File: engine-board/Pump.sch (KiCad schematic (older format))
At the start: 12 parts, among them J301 Steering Turbines, J302 MAXON Pump Controller, J303 Pump Current Sensor, J304 VL6180 Range Sensor, J305 Turbine 1 ESC, J306 Turbine 2 ESC, J307 Turbine Current Sensor, J308 Solenoid Current Sensor, J309 Solenoid, Q301 IRLB8721PBF

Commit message: pcb parts done, footprints updated, ready for routing
pre-routing step..
- finalized footprints
- verified layout, size, mounting holes (1.75" apart)
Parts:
- removed J303: Pump Current Sensor, Connector_PinSocket_2.54mm:PinSocket_1x06_P2.54mm_Vertical, symbol Connector:Conn_01x06_Female
- removed J307: Turbine Current Sensor, Connector_PinSocket_2.54mm:PinSocket_1x06_P2.54mm_Vertical, symbol Connector:Conn_01x06_Female
- removed J308: Solenoid Current Sensor, Connector_PinSocket_2.54mm:PinSocket_1x06_P2.54mm_Vertical, symbol Connector:Conn_01x06_Female
- added J303: Pump Current Sensor, Connector_PinSocket_2.54mm:PinSocket_1x08_P2.54mm_Vertical, symbol Connector:Conn_01x08_Female
- added J307: Turbine Current Sensor, Connector_PinSocket_2.54mm:PinSocket_1x08_P2.54mm_Vertical, symbol Connector:Conn_01x08_Female
- added J308: Solenoid Current Sensor, Connector_PinSocket_2.54mm:PinSocket_1x08_P2.54mm_Vertical, symbol Connector:Conn_01x08_Female
- added TP301: TP_SolGate, TestPoint:TestPoint_Loop_D2.60mm_Drill1.6mm_Beaded, symbol engine-board-eagle-import:TEST-POINTTP_15TH_THRU
- added TP302: TP_SolVolt, TestPoint:TestPoint_Loop_D2.60mm_Drill1.6mm_Beaded, symbol engine-board-eagle-import:TEST-POINTTP_15TH_THRU
- added TP304: TP_SolBat+, TestPoint:TestPoint_Loop_D2.60mm_Drill1.6mm_Beaded, symbol engine-board-eagle-import:TEST-POINTTP_15TH_THRU
- renumbered J302 to J1
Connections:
- wire segments 90 -> 96

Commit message: shortend pcb, ready to route
ready to route, shortend pcb, layout complete
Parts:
- removed TP301: TP_SolGate, TestPoint:TestPoint_Loop_D2.60mm_Drill1.6mm_Beaded, symbol engine-board-eagle-import:TEST-POINTTP_15TH_THRU
- removed TP302: TP_SolVolt, TestPoint:TestPoint_Loop_D2.60mm_Drill1.6mm_Beaded, symbol engine-board-eagle-import:TEST-POINTTP_15TH_THRU
- removed TP304: TP_SolBat+, TestPoint:TestPoint_Loop_D2.60mm_Drill1.6mm_Beaded, symbol engine-board-eagle-import:TEST-POINTTP_15TH_THRU
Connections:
- wire segments 96 -> 93
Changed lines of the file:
@@
 Text HLabel 900  3200 2    50   Input ~ 0
 pump_motor_analog_gnd
-Text HLabel 7950 1000 0    50   Input ~ 0
+Text HLabel 7950 950  0    50   Input ~ 0
 solenoid_mosfet_gate
 $Comp
@@
 	1950 2700 1950 2250
 Connection ~ 2650 2700
-$Comp
-L engine-board-eagle-import:TEST-POINTTP_15TH_THRU TP?
-U 1 1 61D301E8
-P 9600 2000
-AR Path="/61D301E8" Ref="TP?"  Part="1"
-AR Path="/618F9F5D/61D301E8" Ref="TP?"  Part="1"
-AR Path="/619906DF/61D301E8" Ref="TP304"  Part="1"
-F 0 "TP304" H 9644 2240 70  0000 C CNN
-F 1 "TP_SolBat+" H 9644 2119 70  0000 C CNN
-F 2 "TestPoint:TestPoint_Loop_D2.60mm_Drill1.6mm_Beaded" H 9600 2000 50  0001 C CNN
-F 3 "https://www.keyelco.com/userAssets/file/M65p64.pdf" H 9600 2000 50  0001 C CNN
-F 4 "0.23" H 9600 2000 50  0001 C CNN "Price"
-F 5 "680" H 9600 2000 50  0001 C CNN "MFN"
-F 6 "https://www.digikey.com/en/products/detail/keystone-electronics/680/316581" H 9600 2000 50  0001 C CNN "Link"
-	1    9600 2000
-	1    0    0    -1
-$EndComp
-Wire Wire Line
-	9100 1700 9100 2000
-Wire Wire Line
-	9100 2000 9600 2000
-Connection ~ 9100 1700
-$Comp
-L engine-board-eagle-import:TEST-POINTTP_15TH_THRU TP?
-U 1 1 61D3D5E1
-P 9300 1200
-AR Path="/61D3D5E1" Ref="TP?"  Part="1"
-AR Path="/618F9F5D/61D3D5E1" Ref="TP?"  Part="1"
-AR Path="/619906DF/61D3D5E1" Ref="TP302"  Part="1"
-F 0 "TP302" H 9350 1450 70  0000 C CNN
-F 1 "TP_SolVolt" H 9344 1319 70  0000 C CNN
-F 2 "TestPoint:TestPoint_Loop_D2.60mm_Drill1.6mm_Beaded" H 9300 1200 50  0001 C CNN
-F 3 "https://www.keyelco.com/userAssets/file/M65p64.pdf" H 9300 1200 50  0001 C CNN
-F 4 "0.23" H 9300 1200 50  0001 C CNN "Price"
-F 5 "680" H 9300 1200 50  0001 C CNN "MFN"
-F 6 "https://www.digikey.com/en/products/detail/keystone-electronics/680/316581" H 9300 1200 50  0001 C CNN "Link"
-	1    9300 1200
-	1    0    0    -1
-$EndComp
 Connection ~ 9200 1200
-$Comp
-L engine-board-eagle-import:TEST-POINTTP_15TH_THRU TP?
-U 1 1 61D4B1C3
-P 8100 950
-AR Path="/61D4B1C3" Ref="TP?"  Part="1"
-AR Path="/618F9F5D/61D4B1C3" Ref="TP?"  Part="1"
-AR Path="/619906DF/61D4B1C3" Ref="TP301"  Part="1"
-F 0 "TP301" H 8144 1190 70  0000 C CNN
-F 1 "TP_SolGate" H 8144 1069 70  0000 C CNN
-F 2 "TestPoint:TestPoint_Loop_D2.60mm_Drill1.6mm_Beaded" H 8100 950 50  0001 C CNN
-F 3 "https://www.keyelco.com/userAssets/file/M65p64.pdf" H 8100 950 50  0001 C CNN
-F 4 "0.23" H 8100 950 50  0001 C CNN "Price"
-F 5 "680" H 8100 950 50  0001 C CNN "MFN"
-F 6 "https://www.digikey.com/en/products/detail/keystone-electronics/680/316581" H 8100 950 50  0001 C CNN "Link"
-	1    8100 950
-	1    0    0    -1
-$EndComp
 Wire Wire Line
 	9300 1200 9200 1200
 Wire Wire Line
-	7950 950  8100 950
-Wire Wire Line
 	7950 950  7950 1300

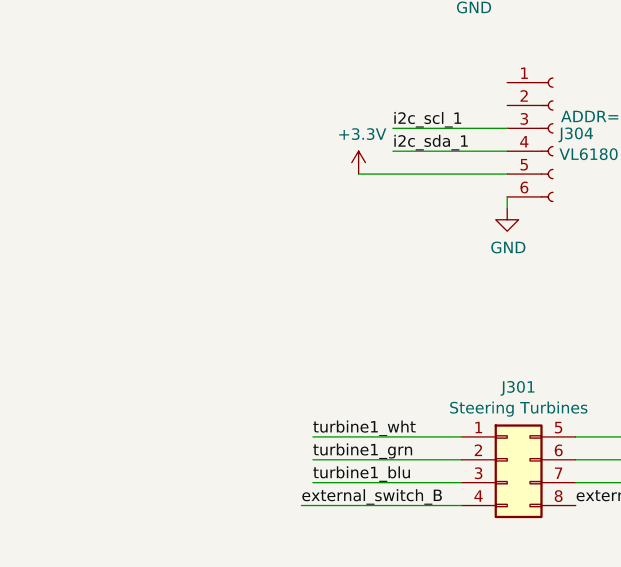
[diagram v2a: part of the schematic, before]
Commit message: ready for layout
- added batt solder tabs
- swapped some terminal blocks with microfit connectors
- shortened board, tightened layout
- tried to space everything out properly
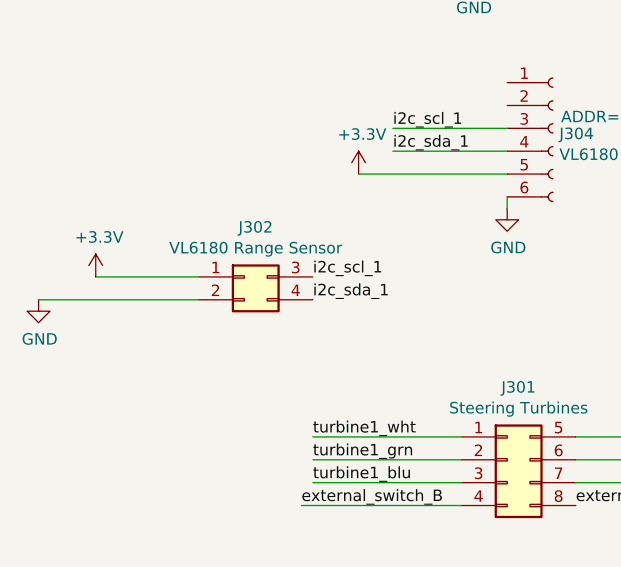
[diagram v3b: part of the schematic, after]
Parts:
- added J302: VL6180 Range Sensor, Connector_Molex:Molex_Micro-Fit_3.0_43045-0421_2x02-1MP_P3.00mm_Horizontal, symbol Connector_Generic:Conn_02x02_Top_Bottom
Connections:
- wire segments 93 -> 95
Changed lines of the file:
@@
 Wire Wire Line
 	7950 950  7950 1300
+$Comp
+L power:GND #PWR?
+U 1 1 62064BBD
+P 850 4650
+AR Path="/618F9F5D/62064BBD" Ref="#PWR?"  Part="1"
+AR Path="/619906DF/62064BBD" Ref="#PWR0116"  Part="1"
+F 0 "#PWR0116" H 850 4400 50  0001 C CNN
+F 1 "GND" H 855 4477 50  0000 C CNN
+F 2 "" H 850 4650 50  0001 C CNN
+F 3 "" H 850 4650 50  0001 C CNN
+	1    850  4650
+	1    0    0    -1
+$EndComp
+Text Label 2050 4550 0    50   ~ 0
+i2c_scl_1
+Text Label 2050 4650 0    50   ~ 0
+i2c_sda_1
+$Comp
+L Connector_Generic:Conn_02x02_Top_Bottom J?
+U 1 1 62064BCC
+P 1750 4550
+AR Path="/618F9F5D/62064BCC" Ref="J?"  Part="1"
+AR Path="/619906DF/62064BCC" Ref="J302"  Part="1"
+F 0 "J302" H 1800 4767 50  0000 C CNN
+F 1 "VL6180 Range Sensor" H 1800 4676 50  0000 C CNN
+F 2 "Connector_Molex:Molex_Micro-Fit_3.0_43045-0421_2x02-1MP_P3.00mm_Horizontal" H 1750 4550 50  0001 C CNN
+F 3 "~" H 1750 4550 50  0001 C CNN
+F 4 "https://www.digikey.com/en/products/detail/molex/0430450422/1635030" H 1750 4550 50  0001 C CNN "Link"
+F 5 "Molex" H 1750 4550 50  0001 C CNN "MANUFACTURER"
+F 6 "0430450422" H 1750 4550 50  0001 C CNN "MPN"
+F 7 "2.38" H 1750 4550 50  0001 C CNN "Price"
+F 8 "430250400" H 1750 4550 50  0001 C CNN "MATE_MPN"
+F 9 "0.48" H 1750 4550 50  0001 C CNN "MATE_Price"
+F 10 "https://www.digikey.com/en/products/detail/molex/0430250400/252497" H 1750 4550 50  0001 C CNN "MATE_Link"
+	1    1750 4550
+	1    0    0    -1
+$EndComp
+Wire Wire Line
+	1100 4550 1550 4550
+Wire Wire Line
+	850  4650 1550 4650
+$Comp
+L power:+3.3V #PWR?
+U 1 1 6206BFFF
+P 1100 4550
+AR Path="/6206BFFF" Ref="#PWR?"  Part="1"
+AR Path="/619906DF/6206BFFF" Ref="#PWR0117"  Part="1"
+F 0 "#PWR0117" H 1100 4400 50  0001 C CNN
+F 1 "+3.3V" H 1115 4723 50  0000 C CNN
+F 2 "" H 1100 4550 50  0001 C CNN
+F 3 "" H 1100 4550 50  0001 C CNN
+	1    1100 4550
+	1    0    0    -1
+$EndComp
 $EndSCHEMATC

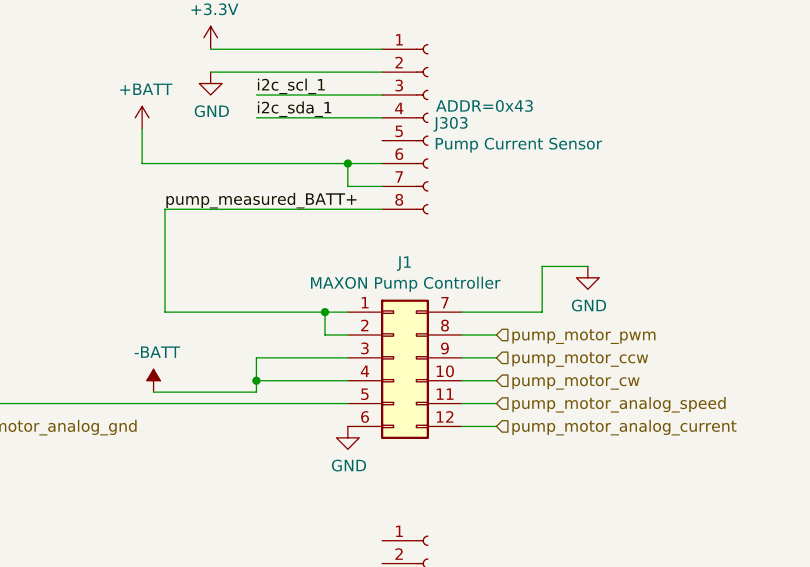
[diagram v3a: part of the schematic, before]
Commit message: ready for routing
- figured out battery input - going with solder strips + sense wires to reduce connector count
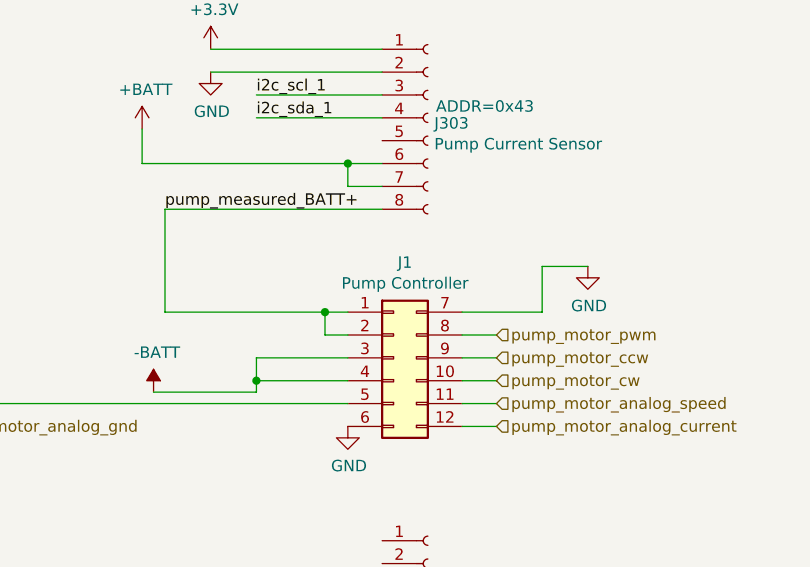
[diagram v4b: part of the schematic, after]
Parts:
- J1: value MAXON Pump Controller -> Pump Controller
- J301: Link (none) -> https://www.digikey.com/short/zjp71dn8; MPM (none) -> 0430450821; Price (none) -> 2.63
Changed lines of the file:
@@
 Wire Wire Line
 	900  3100 2750 3100
-$Comp
-L Connector_Generic:Conn_02x06_Top_Bottom J?
-U 1 1 619BE7D1
-P 2950 2900
-AR Path="/619BE7D1" Ref="J?"  Part="1"
-AR Path="/619906DF/619BE7D1" Ref="J1"  Part="1"
-F 0 "J1" H 3000 3317 50  0000 C CNN
-F 1 "MAXON Pump Controller" H 3000 3226 50  0000 C CNN
-F 2 "TerminalBlock_CUI:CUI_TBP01R1W-508-12BE" H 2950 2900 50  0001 C CNN
-F 3 "~" H 2950 2900 50  0001 C CNN
-F 4 "https://www.digikey.com/en/products/detail/cui-devices/TBP01R1W-508-12BE/10238432" H 2950 2900 50  0001 C CNN "Link"
-F 5 "TBP01R1W-508-12BE" H 2950 2900 50  0001 C CNN "MPN"
-F 6 "CUI Devices" H 2950 2900 50  0001 C CNN "MANUFACTURER"
-F 7 "2.07" H 2950 2900 50  0001 C CNN "Price"
-	1    2950 2900
-	1    0    0    -1
-$EndComp
 Wire Wire Line
 	3600 2500 3600 2700
@@
 F 2 "Connector_Molex:Molex_Micro-Fit_3.0_43045-0821_2x04-1MP_P3.00mm_Horizontal" H 2900 5350 50  0001 C CNN
 F 3 "~" H 2900 5350 50  0001 C CNN
+F 4 "https://www.digikey.com/short/zjp71dn8" H 2900 5350 50  0001 C CNN "Link"
+F 5 "0430450821" H 2900 5350 50  0001 C CNN "MPM"
+F 6 "2.63" H 2900 5350 50  0001 C CNN "Price"
 	1    2900 5350
 	1    0    0    -1
@@
 	1    0    0    -1
 $EndComp
+$Comp
+L Connector_Generic:Conn_02x06_Top_Bottom J?
+U 1 1 619BE7D1
+P 2950 2900
+AR Path="/619BE7D1" Ref="J?"  Part="1"
+AR Path="/619906DF/619BE7D1" Ref="J1"  Part="1"
+F 0 "J1" H 3000 3317 50  0000 C CNN
+F 1 "Pump Controller" H 3000 3226 50  0000 C CNN
+F 2 "TerminalBlock_CUI:CUI_TBP01R1W-508-12BE" H 2950 2900 50  0001 C CNN
+F 3 "~" H 2950 2900 50  0001 C CNN
+F 4 "https://www.digikey.com/en/products/detail/cui-devices/TBP01R1W-508-12BE/10238432" H 2950 2900 50  0001 C CNN "Link"
+F 5 "TBP01R1W-508-12BE" H 2950 2900 50  0001 C CNN "MPN"
+F 6 "CUI Devices" H 2950 2900 50  0001 C CNN "MANUFACTURER"
+F 7 "2.07" H 2950 2900 50  0001 C CNN "Price"
+	1    2950 2900
+	1    0    0    -1
+$EndComp
